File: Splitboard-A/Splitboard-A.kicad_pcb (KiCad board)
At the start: 2 copper layers, 185 x 150 mm, 91 parts, among them J1 USB_C_Receptacle, J2 USB_C_Receptacle_USB2.0, K1 KEYSW, K10 KEYSW, K11 KEYSW, K12 KEYSW, K13 KEYSW, K14 KEYSW, K15 KEYSW, K16 KEYSW, K17 KEYSW, K18 KEYSW, K19 KEYSW, K2 KEYSW, K20 KEYSW, K21 KEYSW, K22 KEYSW, K23 KEYSW, K24 KEYSW, K25 KEYSW, K26 KEYSW, K27 KEYSW, K28 KEYSW, K29 KEYSW, K3 KEYSW, K30 KEYSW, K31 KEYSW, K32 KEYSW, K33 KEYSW, K34 KEYSW, K35 KEYSW, K36 KEYSW, K37 KEYSW, K38 KEYSW, K4 KEYSW, K5 KEYSW, K6 KEYSW, K7 KEYSW, K8 KEYSW, K9 KEYSW, SW1 RotaryEncoder, U1 STM32F407VGTx, U2 AMS1117-3.3, U3 CR2013-MI2120

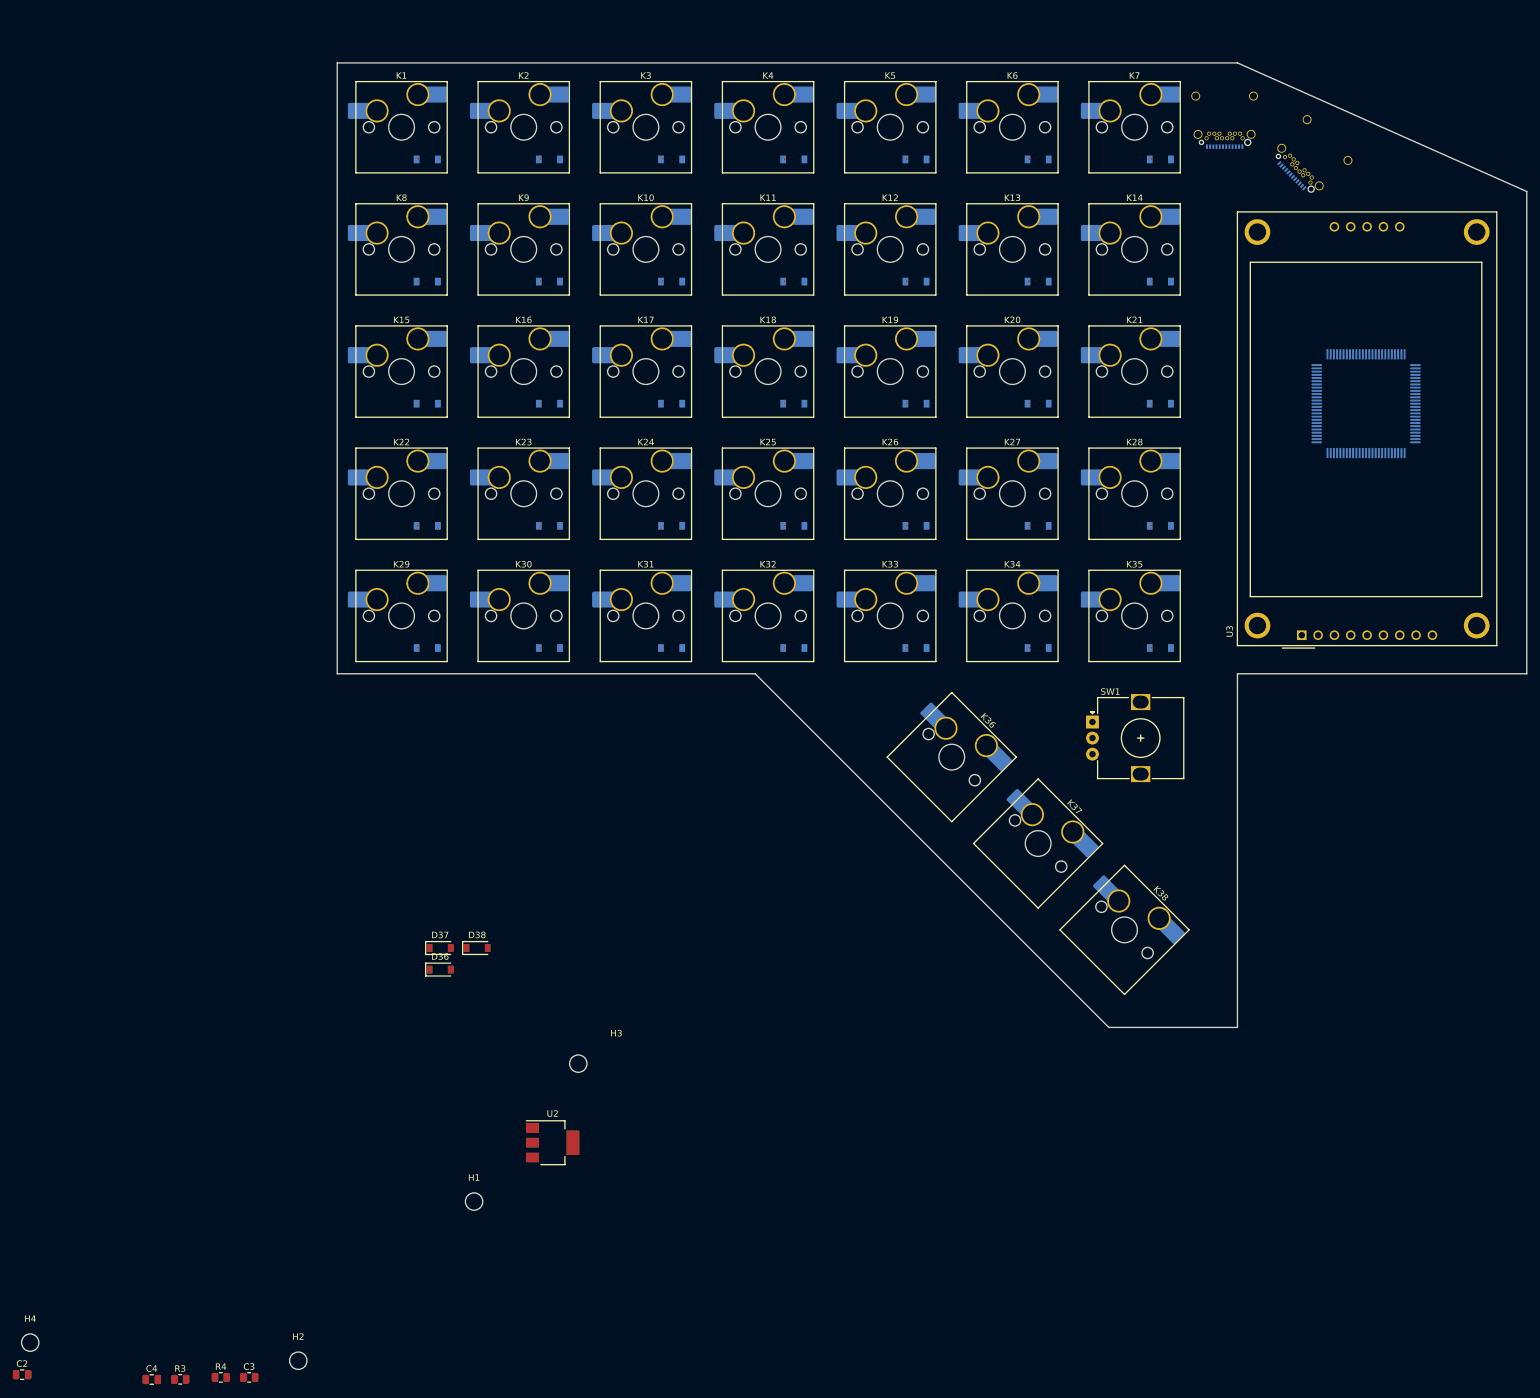
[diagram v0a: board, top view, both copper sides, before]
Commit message: Keyboard changes (added split to other half, component footprints)
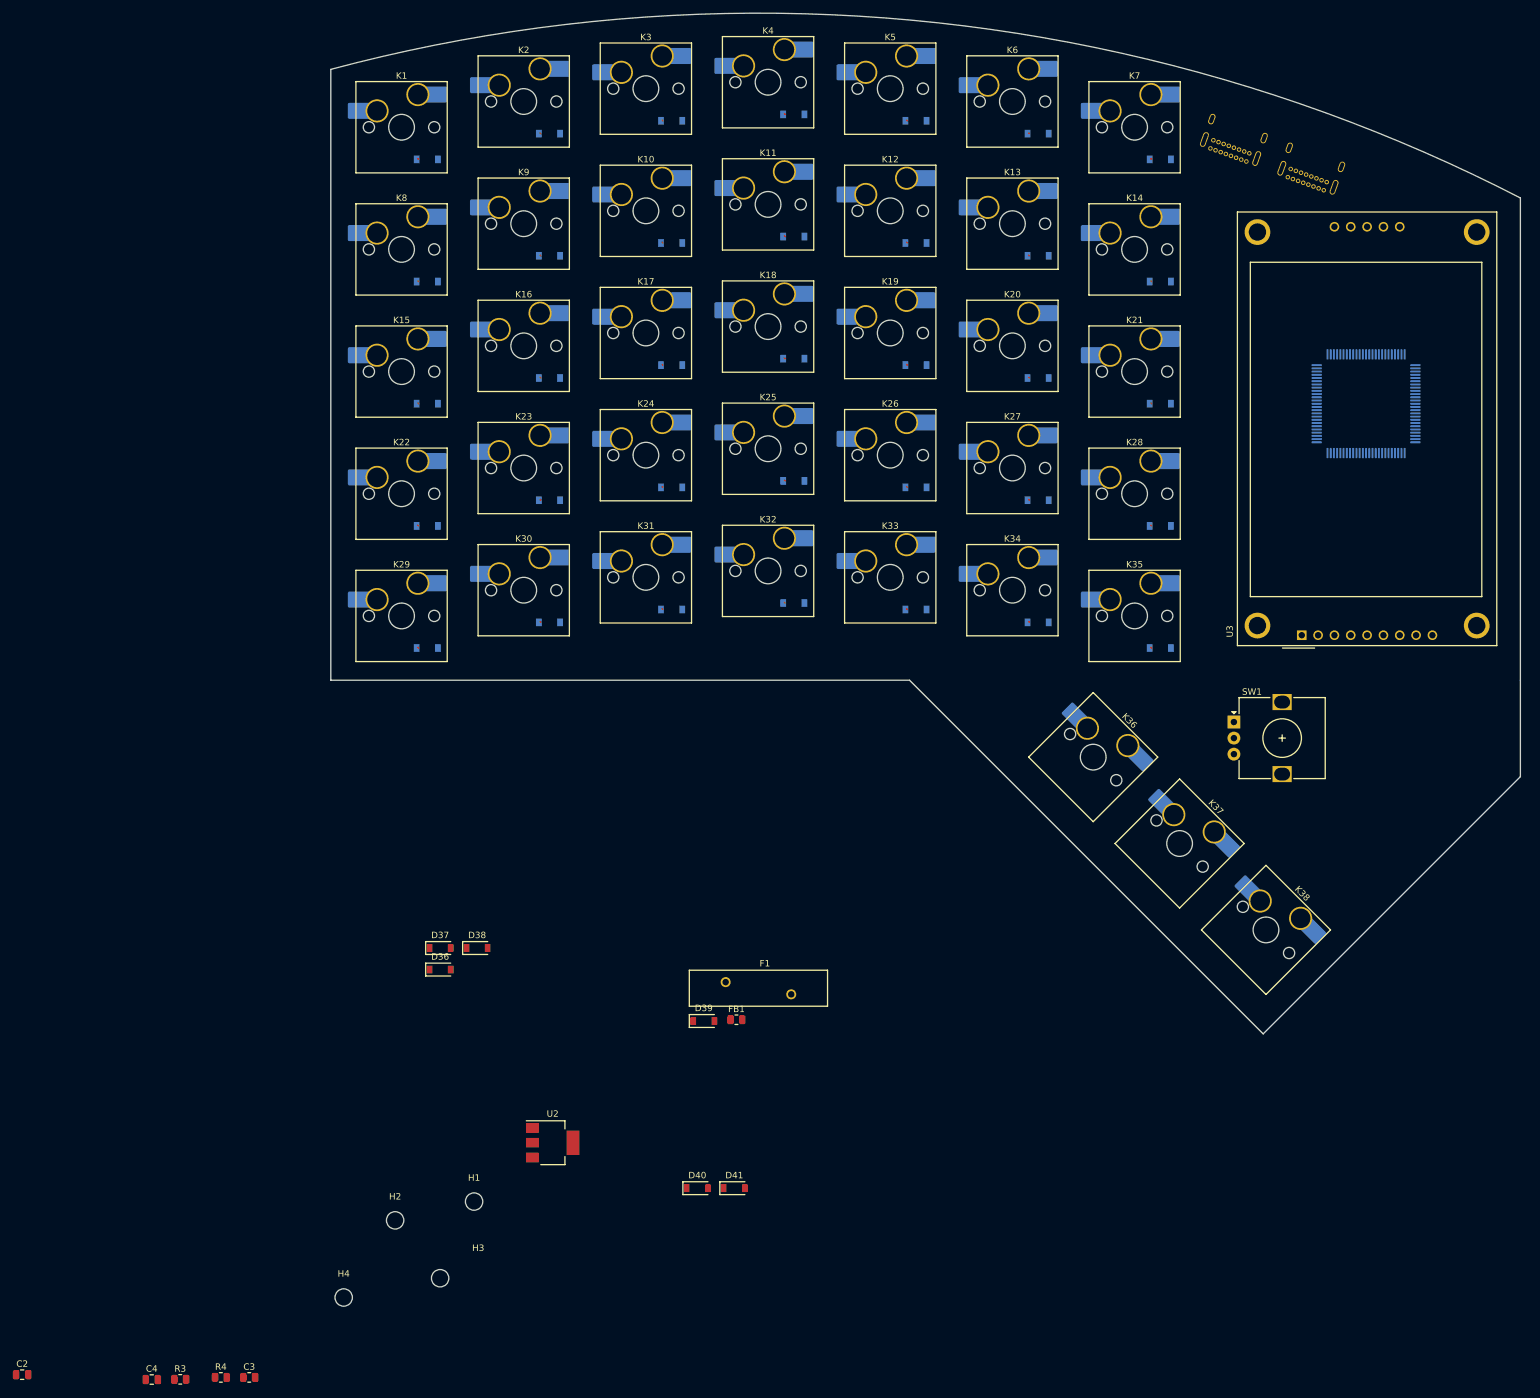
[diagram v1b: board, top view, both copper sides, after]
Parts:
- added D39: D_Schottky, Diode_SMD:D_SOD-123, F.Cu at (152.0, 179.0)
- added D40: D_Schottky, Diode_SMD:D_SOD-123, F.Cu at (151.0, 205.0)
- added D41: D_Schottky, Diode_SMD:D_SOD-123, F.Cu at (156.8, 205.0)
- added F1: 500mA, Fuse:Fuse_BelFuse_0ZRE0125FF_L21.2mm_W5.3mm, F.Cu at (155.4, 172.9)
- added FB1: 100 @ 100 MHz, Resistor_SMD:R_0805_2012Metric, F.Cu at (157.1, 178.8)
- J1, J2: footprint Connector_USB:USB_C_Receptacle_Amphenol_12401548E4-2A_CircularHoles -> Connector_USB:USB_C_Receptacle_GCT_USB4085
- moved H4 49.3 mm to (96.0, 222.0)
- moved H3 39.7 mm to (111.0, 219.0)
- moved H2 26.5 mm to (104.0, 210.0)
- moved K36 22.0 mm to (212.6, 138.0)
- moved K37 22.0 mm to (226.0, 151.4)
- moved K38 22.0 mm to (239.4, 164.8)
- moved SW1 22.0 mm to (234.4, 132.5)
- moved D11 7.00 mm to (166.0, 57.0)
- moved D18 7.00 mm to (166.0, 76.0)
- moved D25 7.00 mm to (166.0, 95.0)
- moved D32 7.00 mm to (166.0, 114.0)
- moved D4 7.00 mm to (166.0, 38.0)
- moved K11 7.00 mm to (162.0, 52.0)
- moved K18 7.00 mm to (162.0, 71.0)
- moved K25 7.00 mm to (162.0, 90.0)
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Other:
- board size 185 x 150 mm -> 185 x 158.7 mm

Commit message: Layout changes
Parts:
- removed D39: D_Schottky, Diode_SMD:D_SOD-123
- added C1: 0.1uF, Resistor_SMD:R_0805_2012Metric, B.Cu at (253.5, 65.5)
- added C10: 100nF, Capacitor_SMD:C_0805_2012Metric, F.Cu at (195.7, 188.1)
- added C11: 100nF, Capacitor_SMD:C_0805_2012Metric, B.Cu at (249.0, 80.5)
- added C12: 100nF, Capacitor_SMD:C_0805_2012Metric, F.Cu at (195.7, 185.1)
- added C13: 100nF, Capacitor_SMD:C_0805_2012Metric, F.Cu at (200.1, 188.1)
- added C14: 100nF, Capacitor_SMD:C_0805_2012Metric, F.Cu at (206.4, 176.1)
- added C15: 100nF, Capacitor_SMD:C_0805_2012Metric, F.Cu at (195.7, 194.1)
- added C16: 100nF, Capacitor_SMD:C_0805_2012Metric, F.Cu at (210.8, 176.1)
- added C17: 100nF, Capacitor_SMD:C_0805_2012Metric, F.Cu at (200.1, 185.1)
- added C5: .01uF, Capacitor_SMD:C_0805_2012Metric, F.Cu at (206.4, 179.1)
- added C6: 100nF, Capacitor_SMD:C_0805_2012Metric, F.Cu at (204.6, 185.1)
- added C7: 100nF, Capacitor_SMD:C_0805_2012Metric, B.Cu at (255.0, 156.0)
- added C8: 1uf, Capacitor_SMD:C_0805_2012Metric, F.Cu at (200.1, 191.1)
- added C9: 100nF, Capacitor_SMD:C_0805_2012Metric, F.Cu at (195.7, 191.1)
- added D42: D_Schottky, Diode_SMD:D_SOD-123, B.Cu at (250.5, 65.5)
- added J3: Conn_01x07, Connector_PinHeader_2.54mm:PinHeader_1x07_P2.54mm_Horizontal, F.Cu at (262.5, 126.0)
- added R1: 10K, Resistor_SMD:R_0805_2012Metric, F.Cu at (215.2, 179.0)
- added R2: 100K, Resistor_SMD:R_0805_2012Metric, F.Cu at (206.3, 182.1)
- added R5: 10k, Resistor_SMD:R_0805_2012Metric, F.Cu at (204.6, 188.0)
- added R6: 10k, Resistor_SMD:R_0805_2012Metric, F.Cu at (210.8, 182.1)
- added SW2: SW_Push, Button_Switch_SMD:Nidec_Copal_SH-7010A, B.Cu at (255.0, 150.5)
- C2, D36, D37, D38, D40, D41, FB1: moved to B.Cu
- C3: value 0.1uF -> 10u; footprint Resistor_SMD:R_0805_2012Metric -> Capacitor_SMD:C_0805_2012Metric; moved to B.Cu
- C4: value 10u -> .01uF
- J1: value USB_C_Receptacle -> USB_C_Receptacle_USB2.0
- J2: value USB_C_Receptacle_USB2.0 -> USB_C_Receptacle
- R3: value 10K -> 10k
- R4: value 100K -> 10k
- U1: value STM32F407VGTx -> AMS1117-3.3; footprint Package_QFP:LQFP-100_14x14mm_P0.5mm -> Package_TO_SOT_SMD:SOT-223-3_TabPin2
- U2: value AMS1117-3.3 -> STM32F407VGTx; footprint Package_TO_SOT_SMD:SOT-223-3_TabPin2 -> Package_QFP:LQFP-100_14x14mm_P0.5mm; moved to B.Cu
- moved C2 271.0 mm to (262.5, 71.0)
- moved C3 236.7 mm to (243.0, 61.5)
- moved D40 187.4 mm to (255.5, 49.5), turned to 90 degrees
- moved D41 173.5 mm to (252.0, 60.0), turned to 180 degrees
- moved U2 171.3 mm to (259.0, 87.0), turned to 180 degrees
- moved F1 163.5 mm to (266.5, 53.0), turned to -90 degrees
- moved FB1 154.1 mm to (260.5, 64.5), turned to -90 degrees
- moved D38 121.9 mm to (238.6, 170.9), turned to -45 degrees
- moved D37 114.7 mm to (225.2, 157.4), turned to -45 degrees
- moved D36 104.3 mm to (211.8, 144.0), turned to -45 degrees
- moved U1 20.4 mm to (243.0, 66.5)
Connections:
- C3 pad 1: Power Regulator -> +3v3 to micro
- C4 pad 1: +3v3 to micro -> /ENC_A
- D40 pad 1: +3.3V -> Net-(D40-Pad1)
- D40 pad 2: Power Regulator -> Voltage Regulator Input
- D41 pad 1: Power Regulator -> +3v3 to micro
- D41 pad 2: GND -> +3v3 to micro
- F1 pad 1: Net-(D39-Pad1) -> Net-(D40-Pad1)
- J1 pad A1: Net-(J1-PadA1) -> GND
- J1 pad A12: Net-(J1-PadA1) -> GND
- J1 pad A4: Net-(J1-PadA4) -> Voltage Regulator Input
- J1 pad A6: unconnected-(J1-PadA6) -> /USB_DP
- J1 pad A7: unconnected-(J1-PadA7) -> /USB_DM
- J1 pad A9: Net-(J1-PadA4) -> Voltage Regulator Input
- J1 pad B1: Net-(J1-PadA1) -> GND
- J1 pad B12: Net-(J1-PadA1) -> GND
- J1 pad B4: Net-(J1-PadA4) -> Voltage Regulator Input
- J1 pad B9: Net-(J1-PadA4) -> Voltage Regulator Input
- J1 pad S1: unconnected-(J1-PadS1) -> GND
- J2 pad A4: /5V -> +3v3 to micro
- J2 pad A9: /5V -> +3v3 to micro
- J2 pad B4: /5V -> +3v3 to micro
- J2 pad B9: /5V -> +3v3 to micro
- R3 pad 1: +3.3V -> +3v3 to micro
- R3 pad 2: Vbus -> Net-(R3-Pad2)
- R4 pad 1: Power Regulator -> /ENC_A
- R4 pad 2: Vbus -> Net-(R3-Pad2)
- SW1 pad A: unconnected-(SW1-PadA) -> Net-(R3-Pad2)
- SW1 pad B: unconnected-(SW1-PadB) -> Net-(R5-Pad1)
- SW1 pad C: unconnected-(SW1-PadC) -> GND
- U1 pad 1: unconnected-(U1-Pad1) -> GND
- U1 pad 2: unconnected-(U1-Pad2) -> +3v3 to micro
- U1 pad 3: unconnected-(U1-Pad3) -> Net-(C2-Pad1)
- U2 pad 1: GND -> unconnected-(U2-Pad1)
- U2 pad 2: +3v3 to micro -> unconnected-(U2-Pad2)
- U2 pad 3: Net-(C2-Pad1) -> unconnected-(U2-Pad3)
- U3 pad 1: unconnected-(U3-Pad1) -> +3v3 to micro
- U3 pad 2: unconnected-(U3-Pad2) -> GND
- U3 pad 3: unconnected-(U3-Pad3) -> /CS
- U3 pad 6: unconnected-(U3-Pad6) -> /MOSI
- U3 pad 7: unconnected-(U3-Pad7) -> /SCK
- U3 pad 9: unconnected-(U3-Pad9) -> /MISO
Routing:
- net /col2: track 0.00 -> 298.0 mm
- net /col1: track 0.00 -> 240.1 mm
- net /row2: track 0.00 -> 211.6 mm
- net GND: track 0.00 -> 208.9 mm
- net /col4: track 0.00 -> 207.8 mm, vias 0 -> 1
- net /row1: track 0.00 -> 197.6 mm
- net /col3: track 0.00 -> 196.0 mm, vias 0 -> 1
- net /row0: track 0.00 -> 194.5 mm
- net /col0: track 0.00 -> 153.8 mm
- net /row6: track 0.00 -> 86.9 mm
- net /row5: track 0.00 -> 86.8 mm
- net /row4: track 0.00 -> 86.8 mm
- net /row3: track 0.00 -> 86.8 mm
- net +3v3 to micro: track 0.00 -> 71.6 mm
- net /col5: track 0.00 -> 67.1 mm, vias 0 -> 1
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
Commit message: Side A layout updates
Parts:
- C10, C12, C13, C14, C15, C16, C17, C4, C5, C6, C8, C9, R1, R2, R3, R4, R5, R6: moved to B.Cu
- moved C4 192.3 mm to (230.6, 135.0)
- moved R3 192.1 mm to (231.0, 129.1), turned to -90 degrees
- moved H1 191.9 mm to (303.3, 164.1)
- moved H2 191.9 mm to (291.0, 167.0)
- moved H3 191.9 mm to (298.0, 176.0)
- moved H4 191.9 mm to (283.0, 179.0)
- moved R4 184.3 mm to (230.5, 132.5)
- moved C13 132.7 mm to (272.0, 76.5), turned to 90 degrees
- moved R2 132.1 mm to (257.0, 60.0), turned to 180 degrees
- moved C12 131.3 mm to (269.5, 76.5), turned to 90 degrees
- moved R1 128.5 mm to (256.9, 57.5), turned to 180 degrees
- moved C15 126.5 mm to (269.0, 91.0), turned to -90 degrees
- moved C9 121.5 mm to (246.0, 80.5), turned to -90 degrees
- moved C10 119.8 mm to (248.5, 80.5), turned to -90 degrees
- moved C8 118.8 mm to (243.5, 80.5), turned to -90 degrees
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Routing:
- net +3v3 to micro: track 71.6 -> 261.6 mm, vias 0 -> 2
- net /row1: track 197.6 -> 339.0 mm, vias 0 -> 2
- net /row2: track 211.6 -> 325.2 mm, vias 0 -> 2
- net /row3: track 86.8 -> 182.1 mm, vias 0 -> 2
- net /col2: track 298.0 -> 205.0 mm, vias 0 -> 1
- net /row0: track 194.5 -> 279.6 mm, vias 0 -> 2
- net /NRST: track 3.91 -> 86.2 mm, vias 0 -> 2
- net /row4: track 86.8 -> 164.3 mm, vias 0 -> 2
- net /SWO: track 0.00 -> 72.4 mm, vias 0 -> 1
- net /SWCLK: track 0.00 -> 68.0 mm, vias 0 -> 1
- net /col0: track 153.8 -> 220.1 mm, vias 0 -> 1
- net /TRST: track 0.00 -> 60.8 mm, vias 0 -> 1
- net /row5: track 86.8 -> 146.9 mm, vias 0 -> 2
- net /SWDIO: track 0.00 -> 59.7 mm, vias 0 -> 1
- net /col5: track 67.1 -> 104.1 mm
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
